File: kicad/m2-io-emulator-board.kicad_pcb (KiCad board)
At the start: 2 copper layers, 180 x 190 mm, 159 parts, among them J1 N2550-6002-RB, J10 61300811121, J11 61301011121, J12 Pin Header 02x18 2.54mm Verti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, J13 VGA femelle, J14 VIDEO, J15 HDMI A, J16 RCJ-2223, J2 N2526-6002-RB, J3 B10P-SHF-1AA, J4 B12P-SHF-1AA, J5 B12P-SHF-1AA, J6 61300811121, J7 61300811121, J8 61300811121, J9 61300811121, SW1 TEST, SW2 SERVICE, U1 ULN2803A, U2 74HCT86, U3 OPA3355EA, U4 CS5213, U5 NX3303X, U6 AT24C02, U7 TS5V330, U8 74HCT157

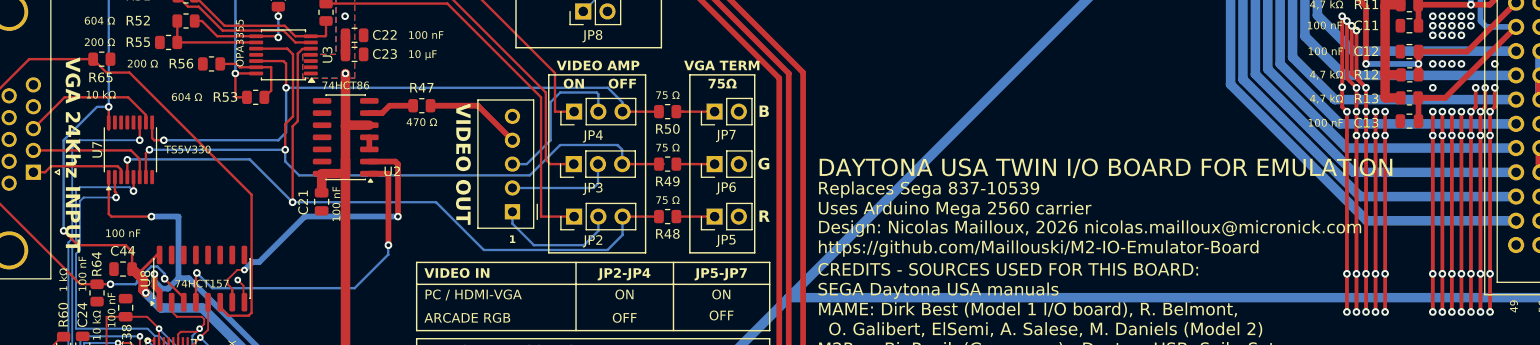
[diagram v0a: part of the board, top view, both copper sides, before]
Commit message: V3: polarity-independent composite sync (Tomi Engdahl's circuit: R66/R67 + C47/C48, all 4 gates of U2), EDID EEPROM U6 and C24 now fitted, "V3" and "24kHz" on the silkscreen; Gerbers, drill files, schematic PDF, 3D renders, BOM (EN/FR) and JLCPCB files (121 SMD) updated
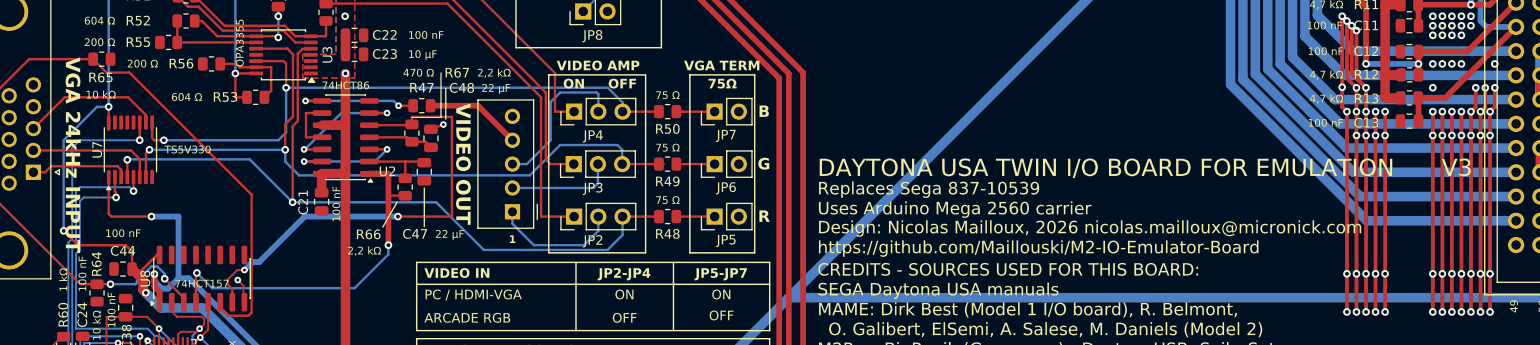
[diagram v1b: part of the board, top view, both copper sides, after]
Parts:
- added C47: 22 µF, Capacitor_SMD:C_0805_2012Metric, F.Cu at (63.3, 134.8)
- added C48: 22 µF, Capacitor_SMD:C_0805_2012Metric, F.Cu at (64.0, 131.3)
- added R66: 2,2 kΩ, Resistor_SMD:R_0805_2012Metric, F.Cu at (61.3, 136.4)
- added R67: 2,2 kΩ, Resistor_SMD:R_0805_2012Metric, F.Cu at (62.0, 130.8)
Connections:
- U2 pad 10: /GND -> /+5V_MEGA
- U2 pad 11: unconnected-(U2-4Y-Pad11) -> /CSYNC_XOR
- U2 pad 12: /GND -> /VS_NORM
- U2 pad 13: /GND -> /HS_NORM
- U2 pad 2: /VGA_VS -> /HS_AVG
- U2 pad 3: /CSYNC_XOR -> /HS_NORM
- U2 pad 4: /CSYNC_XOR -> /VS_AVG
- U2 pad 5: /+5V_MEGA -> /VGA_VS
- U2 pad 6: /CSYNC_N -> /VS_NORM
- U2 pad 8: unconnected-(U2-3Y-Pad8) -> /CSYNC_N
- U2 pad 9: /GND -> /CSYNC_XOR
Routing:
- net /VGA_VS: track 31.6 -> 48.7 mm
- net /VS_NORM: track 0.00 -> 14.0 mm, vias 0 -> 2
- net /HS_NORM: track 0.00 -> 13.0 mm, vias 0 -> 2
- net /CSYNC_N: track 4.91 -> 13.2 mm, vias 0 -> 2
- net /HS_AVG: track 0.00 -> 7.68 mm
- net /VS_AVG: track 0.00 -> 6.88 mm
- net /CSYNC_XOR: track 1.27 -> 5.92 mm
- net /VGA_HS: track 35.8 -> 37.5 mm
- net /GND: track 335.1 -> 336.5 mm, vias 157 -> 158
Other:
- board text added: "V3"
- board text added: "VGA 24kHz INPUT"
- board text removed: "VGA 24Khz INPUT"
